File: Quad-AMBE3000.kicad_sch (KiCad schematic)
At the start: 10 parts, among them U1 74AVC9112DCH, X1 29.4912MHz

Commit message: Most of the layout done
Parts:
- added H1, H2, H3, H4: M3, MountingHole:MountingHole_3.2mm_M3_Pad_Via, symbol Mechanical:MountingHole_Pad
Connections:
- net GND: now also H1.1, H2.1, H3.1, H4.1
- net 3V3_OSC: now reaches C1.2, C2.2, FB1.1, U1.1 (VCC), U1.3 (~{OE}), X1.1 (EN), X1.4 (Vdd)
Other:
- note added: "Mounting Holes"
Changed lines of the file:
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@@
+    (stroke (width 0) (type default))
+  )
+  (wire (pts (xy 71.12 162.56) (xy 71.12 163.83))
     (stroke (width 0) (type default))
   )
@@
     (stroke (width 0) (type default))
   )
+  (wire (pts (xy 97.79 162.56) (xy 97.79 163.83))
+    (stroke (width 0) (type default))
+  )
   (wire (pts (xy 171.45 130.81) (xy 200.66 130.81))
     (stroke (width 0) (type default))
@@
     (stroke (width 0) (type default))
   )
+  (wire (pts (xy 80.01 162.56) (xy 80.01 163.83))
+    (stroke (width 0) (type default))
+  )
   (wire (pts (xy 99.06 111.76) (xy 107.95 111.76))
     (stroke (width 0) (type default))
@@
     (stroke (width 0) (type default))
   )
+  (wire (pts (xy 88.9 162.56) (xy 88.9 163.83))
+    (stroke (width 0) (type default))
+  )
   (wire (pts (xy 125.73 120.65) (xy 132.715 120.65))
     (stroke (width 0) (type default))
@@
   (wire (pts (xy 171.45 67.31) (xy 200.66 67.31))
     (stroke (width 0) (type default))
+  )
+  (rectangle (start 67.31 151.13) (end 105.41 170.18)
+    (stroke (width 0) (type default))
+    (fill (type none))
   )
   (rectangle (start 67.31 99.06) (end 142.24 140.97)
@@
   (text "Clock & Fanout" (at 68.58 104.14 0)
     (effects (font (size 2 2) (thickness 0.4) bold) (justify left bottom))
+  )
+  (text "Mounting Holes" (at 68.58 154.94 0)
+    (effects (font (size 2 2) (thickness 0.4) bold) (justify left bottom))
+  )
+  (label "3V3_OSC" (at 87.63 111.76 0) (fields_autoplaced)
+    (effects (font (size 1.27 1.27)) (justify left bottom))
   )
   (global_label "CLK_B" (shape input) (at 196.85 97.79 180) (fields_autoplaced)
@@
     )
   )
+  (symbol (lib_id "Mechanical:MountingHole_Pad") (at 80.01 160.02 0) (unit 1)
+    (in_bom yes) (on_board yes) (dnp no) (fields_autoplaced)
+    (property "Reference" "H2" (at 82.55 157.48 0)
+      (effects (font (size 1.27 1.27)) (justify left))
+    )
+    (property "Value" "M3" (at 82.55 160.02 0)
+      (effects (font (size 1.27 1.27)) (justify left))
+    )
+    (property "Footprint" "MountingHole:MountingHole_3.2mm_M3_Pad_Via" (at 80.01 160.02 0)
+      (effects (font (size 1.27 1.27)) hide)
+    )
+    (property "Datasheet" "~" (at 80.01 160.02 0)
+      (effects (font (size 1.27 1.27)) hide)
+    )
+    (pin "1")
+    (instances
+      (project "Quad-AMBE3000"
+        (path "/5724fa40-164f-4058-9cc8-ef80d9809dcd"
+          (reference "H2") (unit 1)
+        )
+      )
+    )
+  )
   (symbol (lib_id "Device:R_Small") (at 123.19 123.19 90) (unit 1)
     (in_bom yes) (on_board yes) (dnp no)
@@
     )
   )
+  (symbol (lib_id "power:GND") (at 71.12 163.83 0) (unit 1)
+    (in_bom yes) (on_board yes) (dnp no)
+    (property "Reference" "#PWR091" (at 71.12 170.18 0)
+      (effects (font (size 1.27 1.27)) hide)
+    )
+    (property "Value" "GND" (at 71.12 167.64 0)
+      (effects (font (size 1.27 1.27)))
+    )
+    (property "Footprint" "" (at 71.12 163.83 0)
+      (effects (font (size 1.27 1.27)) hide)
+    )
+    (property "Datasheet" "" (at 71.12 163.83 0)
+      (effects (font (size 1.27 1.27)) hide)
+    )
+    (pin "1")
+    (instances
+      (project "Quad-AMBE3000"
+        (path "/5724fa40-164f-4058-9cc8-ef80d9809dcd"
+          (reference "#PWR091") (unit 1)
+        )
+      )
+    )
+  )
   (symbol (lib_id "Oscillator:ASV-xxxMHz") (at 83.82 120.65 0) (unit 1)
     (in_bom yes) (on_board yes) (dnp no)
@@
         (path "/5724fa40-164f-4058-9cc8-ef80d9809dcd"
           (reference "X1") (unit 1)
+        )
+      )
+    )
+  )
+  (symbol (lib_id "power:GND") (at 97.79 163.83 0) (unit 1)
+    (in_bom yes) (on_board yes) (dnp no)
+    (property "Reference" "#PWR0125" (at 97.79 170.18 0)
+      (effects (font (size 1.27 1.27)) hide)
+    )
+    (property "Value" "GND" (at 97.79 167.64 0)
+      (effects (font (size 1.27 1.27)))
+    )
+    (property "Footprint" "" (at 97.79 163.83 0)
+      (effects (font (size 1.27 1.27)) hide)
+    )
+    (property "Datasheet" "" (at 97.79 163.83 0)
+      (effects (font (size 1.27 1.27)) hide)
+    )
+    (pin "1")
+    (instances
+      (project "Quad-AMBE3000"
+        (path "/5724fa40-164f-4058-9cc8-ef80d9809dcd"
+          (reference "#PWR0125") (unit 1)
+        )
+      )
+    )
+  )
+  (symbol (lib_id "Mechanical:MountingHole_Pad") (at 97.79 160.02 0) (unit 1)
+    (in_bom yes) (on_board yes) (dnp no) (fields_autoplaced)
+    (property "Reference" "H4" (at 100.33 157.48 0)
+      (effects (font (size 1.27 1.27)) (justify left))
+    )
+    (property "Value" "M3" (at 100.33 160.02 0)
+      (effects (font (size 1.27 1.27)) (justify left))
+    )
+    (property "Footprint" "MountingHole:MountingHole_3.2mm_M3_Pad_Via" (at 97.79 160.02 0)
+      (effects (font (size 1.27 1.27)) hide)
+    )
+    (property "Datasheet" "~" (at 97.79 160.02 0)
+      (effects (font (size 1.27 1.27)) hide)
+    )
+    (pin "1")
+    (instances
+      (project "Quad-AMBE3000"
+        (path "/5724fa40-164f-4058-9cc8-ef80d9809dcd"
+          (reference "H4") (unit 1)
+        )
+      )
+    )
+  )
+  (symbol (lib_id "power:GND") (at 80.01 163.83 0) (unit 1)
+    (in_bom yes) (on_board yes) (dnp no)
+    (property "Reference" "#PWR094" (at 80.01 170.18 0)
+      (effects (font (size 1.27 1.27)) hide)
+    )
+    (property "Value" "GND" (at 80.01 167.64 0)
+      (effects (font (size 1.27 1.27)))
+    )
+    (property "Footprint" "" (at 80.01 163.83 0)
+      (effects (font (size 1.27 1.27)) hide)
+    )
+    (property "Datasheet" "" (at 80.01 163.83 0)
+      (effects (font (size 1.27 1.27)) hide)
+    )
+    (pin "1")
+    (instances
+      (project "Quad-AMBE3000"
+        (path "/5724fa40-164f-4058-9cc8-ef80d9809dcd"
+          (reference "#PWR094") (unit 1)
         )
       )
@@
     )
   )
+  (symbol (lib_id "Mechanical:MountingHole_Pad") (at 71.12 160.02 0) (unit 1)
+    (in_bom yes) (on_board yes) (dnp no) (fields_autoplaced)
+    (property "Reference" "H1" (at 73.66 157.48 0)
+      (effects (font (size 1.27 1.27)) (justify left))
+    )
+    (property "Value" "M3" (at 73.66 160.02 0)
+      (effects (font (size 1.27 1.27)) (justify left))
+    )
+    (property "Footprint" "MountingHole:MountingHole_3.2mm_M3_Pad_Via" (at 71.12 160.02 0)
+      (effects (font (size 1.27 1.27)) hide)
+    )
+    (property "Datasheet" "~" (at 71.12 160.02 0)
+      (effects (font (size 1.27 1.27)) hide)
+    )
+    (pin "1")
+    (instances
+      (project "Quad-AMBE3000"
+        (path "/5724fa40-164f-4058-9cc8-ef80d9809dcd"
+          (reference "H1") (unit 1)
+        )
+      )
+    )
+  )
   (symbol (lib_id "Device:C_Small") (at 99.06 132.08 0) (mirror x) (unit 1)
     (in_bom yes) (on_board yes) (dnp no)
@@
     )
   )
+  (symbol (lib_id "power:GND") (at 88.9 163.83 0) (unit 1)
+    (in_bom yes) (on_board yes) (dnp no)
+    (property "Reference" "#PWR0122" (at 88.9 170.18 0)
+      (effects (font (size 1.27 1.27)) hide)
+    )
+    (property "Value" "GND" (at 88.9 167.64 0)
+      (effects (font (size 1.27 1.27)))
+    )
+    (property "Footprint" "" (at 88.9 163.83 0)
+      (effects (font (size 1.27 1.27)) hide)
+    )
+    (property "Datasheet" "" (at 88.9 163.83 0)
+      (effects (font (size 1.27 1.27)) hide)
+    )
+    (pin "1")
+    (instances
+      (project "Quad-AMBE3000"
+        (path "/5724fa40-164f-4058-9cc8-ef80d9809dcd"
+          (reference "#PWR0122") (unit 1)
+        )
+      )
+    )
+  )
   (symbol (lib_id "power:GND") (at 107.95 133.35 0) (mirror y) (unit 1)
     (in_bom yes) (on_board yes) (dnp no)
@@
         )
       )
+    )
+  )
+  (symbol (lib_id "Mechanical:MountingHole_Pad") (at 88.9 160.02 0) (unit 1)
+    (in_bom yes) (on_board yes) (dnp no) (fields_autoplaced)
+    (property "Reference" "H3" (at 91.44 157.48 0)
+      (effects (font (size 1.27 1.27)) (justify left))
+    )
+    (property "Value" "M3" (at 91.44 160.02 0)
+      (effects (font (size 1.27 1.27)) (justify left))
+    )
+    (property "Footprint" "MountingHole:MountingHole_3.2mm_M3_Pad_Via" (at 88.9 160.02 0)
+      (effects (font (size 1.27 1.27)) hide)
+    )
+    (property "Datasheet" "~" (at 88.9 160.02 0)
+      (effects (font (size 1.27 1.27)) hide)
+    )
+    (pin "1")
+    (instances
+      (project "Quad-AMBE3000"
+        (path "/5724fa40-164f-4058-9cc8-ef80d9809dcd"
+          (reference "H3") (unit 1)
+        )
+      )

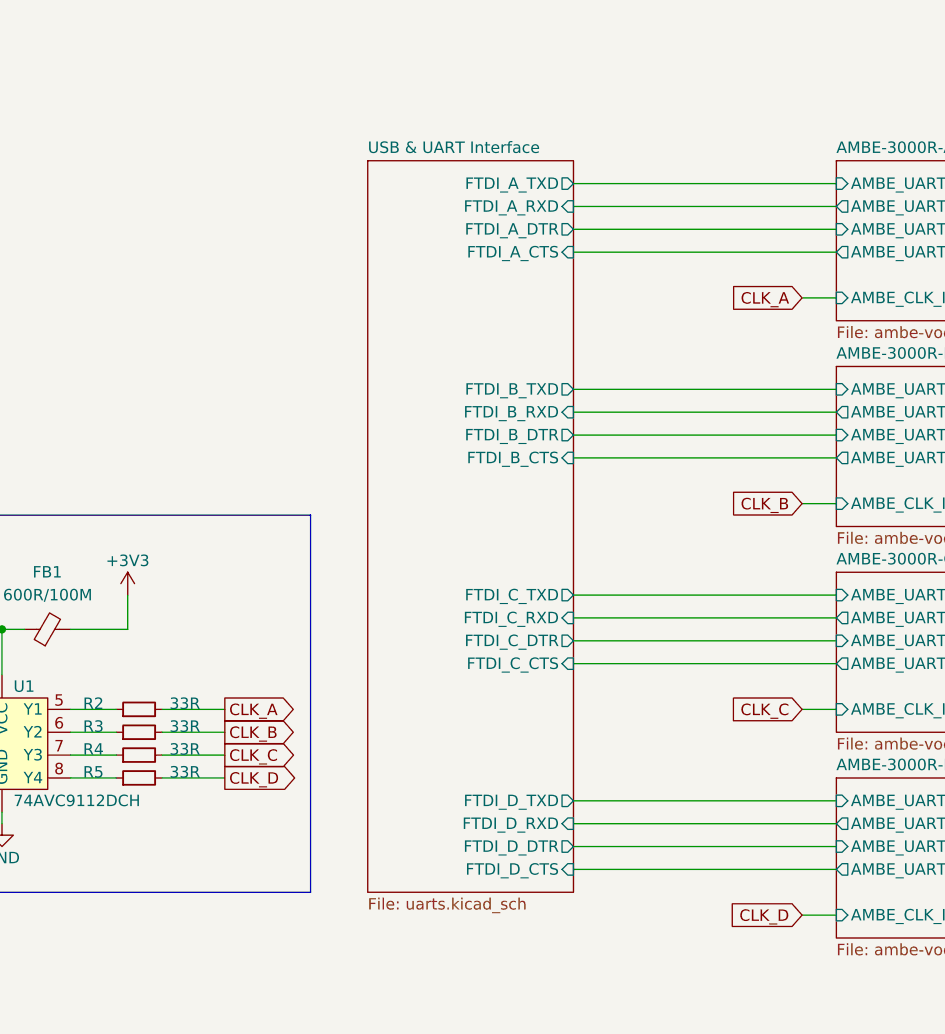
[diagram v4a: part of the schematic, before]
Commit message: Routing finished. Need to tidy DRC & BoM
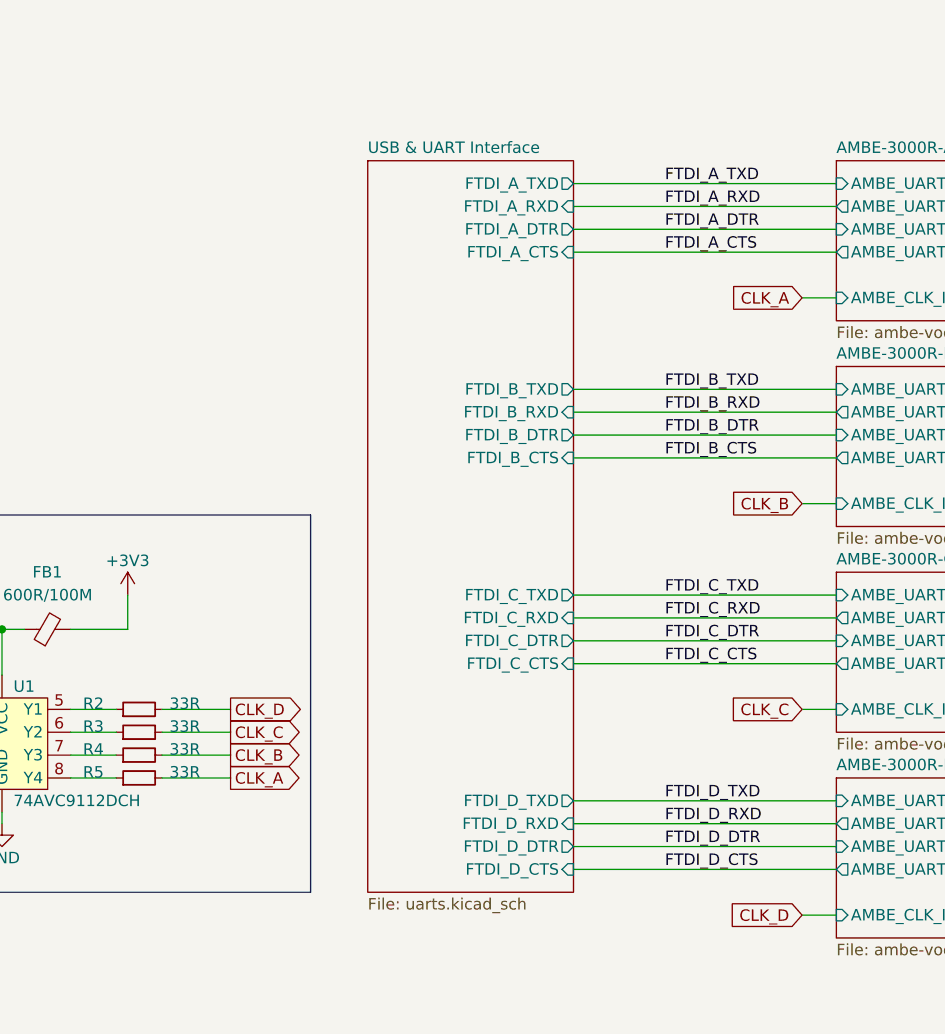
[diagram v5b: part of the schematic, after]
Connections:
- net CLK_A: now also R5.2; no longer R2.2
- net CLK_B: now also R4.2; no longer R3.2
- net CLK_C: now also R3.2; no longer R4.2
- net CLK_D: now also R2.2; no longer R5.2

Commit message: Final updates before manufacture of V1.00
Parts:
- C1, C2: LCSC (none) -> C14663
- H1, H2, H3, H4: LCSC (none) -> DNF
- R1, R2, R3, R4, R5: LCSC (none) -> C23140
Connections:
- net GND: now also U1.3 (~{OE})
- net +3V3 renamed +1V8
- net 3V3_OSC renamed 1V8_OSC
- net 1V8_OSC: no longer U1.3 (~{OE})
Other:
- note added: "AMBE-3000R clock input is 1V8"
- note added: "George Smart, M1GEO. Chris Smart, G8OCV. https://github.com/m1geo/Quad-AMBE3000"
- note removed: "George Smart, M1GEO. https://github.com/m1geo/Quad-AMBE3000"
- title: Quad AMBE-3000R Board -> Quad AMBE-3000R Board (Top)
- moved on the sheet: C2
